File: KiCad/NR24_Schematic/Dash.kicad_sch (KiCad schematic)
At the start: 11 parts, among them J9 AEM Dash, SW2 Shifter Switch, SW5 Key Switch, SW6 12V E-stop

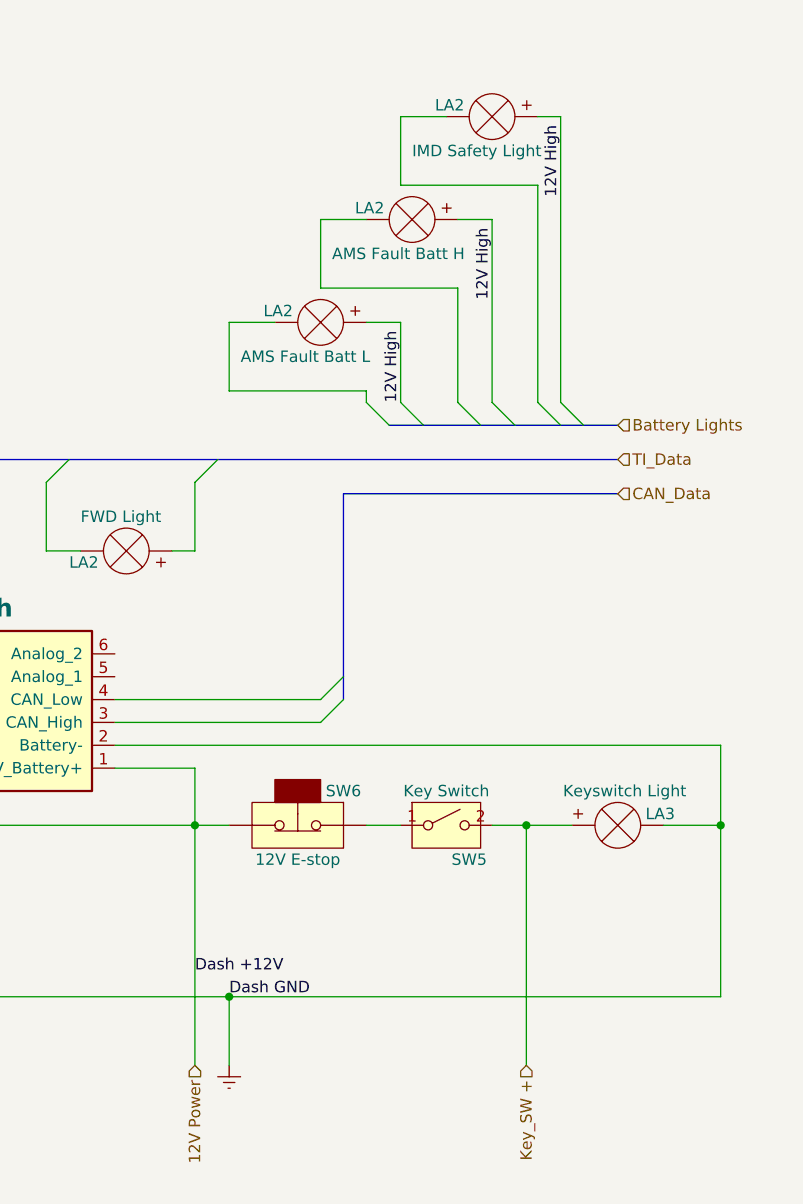
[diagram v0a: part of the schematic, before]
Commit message: added accumulator info
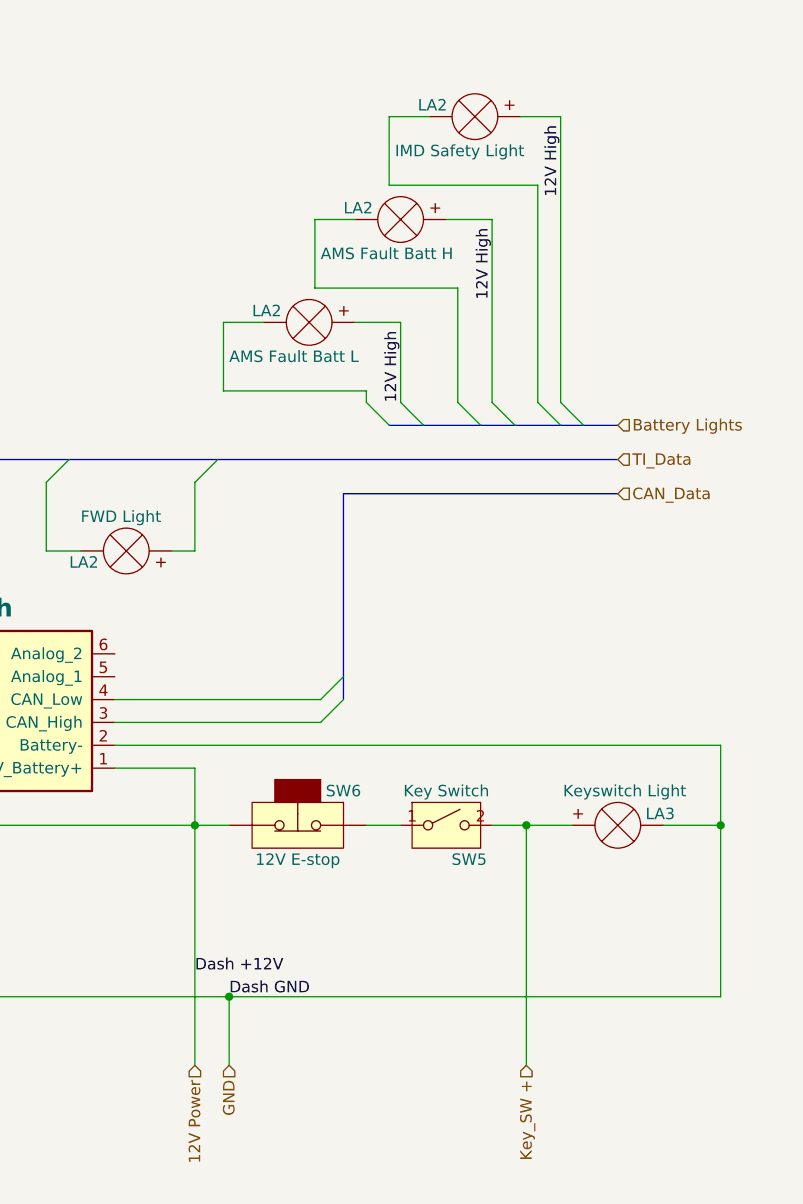
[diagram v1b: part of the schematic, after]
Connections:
- net Earth renamed GND
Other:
- moved on the sheet: LA2
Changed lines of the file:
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@@
     (stroke (width 0) (type default))
   )
-  (wire (pts (xy 187.96 46.99) (xy 187.96 54.61))
+  (wire (pts (xy 187.325 46.99) (xy 187.325 54.61))
     (stroke (width 0) (type default))
   )
@@
     (stroke (width 0) (type default))
   )
-  (wire (pts (xy 217.17 35.56) (xy 213.36 35.56))
+  (wire (pts (xy 217.17 35.56) (xy 212.09 35.56))
     (stroke (width 0) (type default))
   )
@@
     (stroke (width 0) (type default))
   )
-  (wire (pts (xy 187.96 54.61) (xy 203.2 54.61))
-    (stroke (width 0) (type default))
-  )
-  (wire (pts (xy 193.04 46.99) (xy 187.96 46.99))
+  (wire (pts (xy 187.325 54.61) (xy 203.2 54.61))
+    (stroke (width 0) (type default))
+  )
+  (wire (pts (xy 191.77 46.99) (xy 187.325 46.99))
     (stroke (width 0) (type default))
   )
@@
     (stroke (width 0) (type default))
   )
-  (wire (pts (xy 198.12 43.18) (xy 213.36 43.18))
+  (wire (pts (xy 197.485 43.18) (xy 213.36 43.18))
     (stroke (width 0) (type default))
   )
@@
     (stroke (width 0) (type default))
   )
-  (wire (pts (xy 207.01 24.13) (xy 207.01 31.75))
+  (wire (pts (xy 205.74 24.13) (xy 205.74 31.75))
     (stroke (width 0) (type default))
   )
@@
     (stroke (width 0) (type default))
   )
-  (wire (pts (xy 198.12 35.56) (xy 198.12 43.18))
-    (stroke (width 0) (type default))
-  )
-  (wire (pts (xy 222.25 24.13) (xy 224.79 24.13))
+  (wire (pts (xy 197.485 35.56) (xy 197.485 43.18))
+    (stroke (width 0) (type default))
+  )
+  (wire (pts (xy 220.345 24.13) (xy 224.79 24.13))
     (stroke (width 0) (type default))
   )
@@
     (stroke (width 0) (type default))
   )
-  (wire (pts (xy 207.01 46.99) (xy 203.2 46.99))
+  (wire (pts (xy 207.01 46.99) (xy 201.93 46.99))
     (stroke (width 0) (type default))
   )
@@
     (stroke (width 0) (type default))
   )
-  (wire (pts (xy 212.09 24.13) (xy 207.01 24.13))
-    (stroke (width 0) (type default))
-  )
-  (wire (pts (xy 207.01 31.75) (xy 222.25 31.75))
+  (wire (pts (xy 210.185 24.13) (xy 205.74 24.13))
+    (stroke (width 0) (type default))
+  )
+  (wire (pts (xy 205.74 31.75) (xy 222.25 31.75))
     (stroke (width 0) (type default))
   )
@@
     (stroke (width 0) (type default))
   )
-  (wire (pts (xy 203.2 35.56) (xy 198.12 35.56))
+  (wire (pts (xy 201.93 35.56) (xy 197.485 35.56))
     (stroke (width 0) (type default))
   )
@@
     (effects (font (size 1.27 1.27)) (justify right))
   )
+  (hierarchical_label "GND" (shape input) (at 187.96 129.54 270) (fields_autoplaced)
+    (effects (font (size 1.27 1.27)) (justify right))
+  )
   (hierarchical_label "CAN_Data" (shape input) (at 231.14 66.04 0) (fields_autoplaced)
     (effects (font (size 1.27 1.27)) (justify left))
@@
     (pin "2")
     (instances
-      (project "Car_TractiveSystem_v2"
+      (project "Car_TractiveSystem_MAIN"
         (path "/588b5c14-1813-4e1d-9dbe-940839ecebe3"
           (reference "LA3") (unit 1)
@@
     (pin "2")
     (instances
-      (project "Car_TractiveSystem_v2"
+      (project "Car_TractiveSystem_MAIN"
         (path "/588b5c14-1813-4e1d-9dbe-940839ecebe3"
           (reference "SW5") (unit 1)
@@
     (pin "2")
     (instances
-      (project "Car_TractiveSystem_v2"
+      (project "Car_TractiveSystem_MAIN"
         (path "/588b5c14-1813-4e1d-9dbe-940839ecebe3"
           (reference "LA2") (unit 1)
@@
     )
   )
-  (symbol (lib_name "Lamp_2") (lib_id "Device:Lamp") (at 187.96 48.26 0) (mirror y) (unit 1)
-    (in_bom yes) (on_board yes) (dnp no)
-    (property "Reference" "LA2" (at 191.77 45.72 0)
-      (effects (font (size 1.27 1.27)) (justify right))
-    )
-    (property "Value" "AMS Fault Batt L" (at 189.23 50.8 0)
-      (effects (font (size 1.27 1.27)) (justify right))
-    )
-    (property "Footprint" "" (at 195.58 46.99 0)
-      (effects (font (size 1.27 1.27)) hide)
-    )
-    (property "Datasheet" "~" (at 195.58 46.99 0)
-      (effects (font (size 1.27 1.27)) hide)
-    )
-    (pin "1")
-    (pin "2")
-    (instances
-      (project "Car_TractiveSystem_v2"
+  (symbol (lib_name "Lamp_2") (lib_id "Device:Lamp") (at 186.69 48.26 0) (mirror y) (unit 1)
+    (in_bom yes) (on_board yes) (dnp no)
+    (property "Reference" "LA2" (at 190.5 45.72 0)
+      (effects (font (size 1.27 1.27)) (justify right))
+    )
+    (property "Value" "AMS Fault Batt L" (at 187.96 50.8 0)
+      (effects (font (size 1.27 1.27)) (justify right))
+    )
+    (property "Footprint" "" (at 194.31 46.99 0)
+      (effects (font (size 1.27 1.27)) hide)
+    )
+    (property "Datasheet" "~" (at 194.31 46.99 0)
+      (effects (font (size 1.27 1.27)) hide)
+    )
+    (pin "1")
+    (pin "2")
+    (instances
+      (project "Car_TractiveSystem_MAIN"
         (path "/588b5c14-1813-4e1d-9dbe-940839ecebe3"
           (reference "LA2") (unit 1)
@@
     (pin "8")
     (instances
-      (project "Car_TractiveSystem_v2"
+      (project "Car_TractiveSystem_MAIN"
         (path "/588b5c14-1813-4e1d-9dbe-940839ecebe3"
           (reference "SW2") (unit 1)
@@
     (pin "2")
     (instances
-      (project "Car_TractiveSystem_v2"
+      (project "Car_TractiveSystem_MAIN"
         (path "/588b5c14-1813-4e1d-9dbe-940839ecebe3"
           (reference "LA5") (unit 1)
@@
     (pin "2")
     (instances
-      (project "Car_TractiveSystem_v2"
+      (project "Car_TractiveSystem_MAIN"
         (path "/588b5c14-1813-4e1d-9dbe-940839ecebe3"
           (reference "LA1") (unit 1)
@@
     (pin "2")
     (instances
-      (project "Car_TractiveSystem_v2"
+      (project "Car_TractiveSystem_MAIN"
         (path "/588b5c14-1813-4e1d-9dbe-940839ecebe3"
           (reference "SW6") (unit 1)
@@
     )
   )
-  (symbol (lib_id "power:Earth") (at 187.96 129.54 0) (unit 1)
-    (in_bom yes) (on_board yes) (dnp no) (fields_autoplaced)
-    (property "Reference" "#PWR01" (at 187.96 135.89 0)
-      (effects (font (size 1.27 1.27)) hide)
-    )
-    (property "Value" "Earth" (at 187.96 133.35 0)
-      (effects (font (size 1.27 1.27)) hide)
-    )
-    (property "Footprint" "" (at 187.96 129.54 0)
-      (effects (font (size 1.27 1.27)) hide)
-    )
-    (property "Datasheet" "~" (at 187.96 129.54 0)
-      (effects (font (size 1.27 1.27)) hide)
-    )
-    (pin "1")
-    (instances
-      (project "Car_TractiveSystem_v2"
-        (path "/588b5c14-1813-4e1d-9dbe-940839ecebe3"
-          (reference "#PWR01") (unit 1)
-        )
-        (path "/588b5c14-1813-4e1d-9dbe-940839ecebe3/62b4fa84-4530-4bff-bc03-eb6ea850cb52"
-          (reference "#PWR05") (unit 1)
-        )
-      )
-    )
-  )
-  (symbol (lib_name "Lamp_2") (lib_id "Device:Lamp") (at 207.01 25.4 0) (mirror y) (unit 1)
-    (in_bom yes) (on_board yes) (dnp no)
-    (property "Reference" "LA2" (at 210.82 22.86 0)
-      (effects (font (size 1.27 1.27)) (justify right))
-    )
-    (property "Value" "IMD Safety Light" (at 208.28 27.94 0)
-      (effects (font (size 1.27 1.27)) (justify right))
-    )
-    (property "Footprint" "" (at 214.63 24.13 0)
-      (effects (font (size 1.27 1.27)) hide)
-    )
-    (property "Datasheet" "~" (at 214.63 24.13 0)
-      (effects (font (size 1.27 1.27)) hide)
-    )
-    (pin "1")
-    (pin "2")
-    (instances
-      (project "Car_TractiveSystem_v2"
+  (symbol (lib_name "Lamp_2") (lib_id "Device:Lamp") (at 205.105 25.4 0) (mirror y) (unit 1)
+    (in_bom yes) (on_board yes) (dnp no)
+    (property "Reference" "LA2" (at 208.915 22.86 0)
+      (effects (font (size 1.27 1.27)) (justify right))
+    )
+    (property "Value" "IMD Safety Light" (at 206.375 27.94 0)
+      (effects (font (size 1.27 1.27)) (justify right))
+    )
+    (property "Footprint" "" (at 212.725 24.13 0)
+      (effects (font (size 1.27 1.27)) hide)
+    )
+    (property "Datasheet" "~" (at 212.725 24.13 0)
+      (effects (font (size 1.27 1.27)) hide)
+    )
+    (pin "1")
+    (pin "2")
+    (instances
+      (project "Car_TractiveSystem_MAIN"
         (path "/588b5c14-1813-4e1d-9dbe-940839ecebe3"
           (reference "LA2") (unit 1)
@@
     (pin "9")
     (instances
-      (project "Car_TractiveSystem_v2"
+      (project "Car_TractiveSystem_MAIN"
         (path "/588b5c14-1813-4e1d-9dbe-940839ecebe3/62b4fa84-4530-4bff-bc03-eb6ea850cb52"
           (reference "J9") (unit 1)
@@
     )
   )
-  (symbol (lib_name "Lamp_2") (lib_id "Device:Lamp") (at 198.12 36.83 0) (mirror y) (unit 1)
-    (in_bom yes) (on_board yes) (dnp no)
-    (property "Reference" "LA2" (at 201.93 34.29 0)
-      (effects (font (size 1.27 1.27)) (justify right))
-    )
-    (property "Value" "AMS Fault Batt H" (at 199.39 39.37 0)
-      (effects (font (size 1.27 1.27)) (justify right))
-    )
-    (property "Footprint" "" (at 205.74 35.56 0)
-      (effects (font (size 1.27 1.27)) hide)
-    )
-    (property "Datasheet" "~" (at 205.74 35.56 0)
-      (effects (font (size 1.27 1.27)) hide)
-    )
-    (pin "1")
-    (pin "2")
-    (instances
-      (project "Car_TractiveSystem_v2"
+  (symbol (lib_name "Lamp_2") (lib_id "Device:Lamp") (at 196.85 36.83 0) (mirror y) (unit 1)
+    (in_bom yes) (on_board yes) (dnp no)
+    (property "Reference" "LA2" (at 200.66 34.29 0)
+      (effects (font (size 1.27 1.27)) (justify right))
+    )
+    (property "Value" "AMS Fault Batt H" (at 198.12 39.37 0)
+      (effects (font (size 1.27 1.27)) (justify right))
+    )
+    (property "Footprint" "" (at 204.47 35.56 0)
+      (effects (font (size 1.27 1.27)) hide)
+    )
+    (property "Datasheet" "~" (at 204.47 35.56 0)
+      (effects (font (size 1.27 1.27)) hide)
+    )
+    (pin "1")
+    (pin "2")
+    (instances
+      (project "Car_TractiveSystem_MAIN"
         (path "/588b5c14-1813-4e1d-9dbe-940839ecebe3"
           (reference "LA2") (unit 1)

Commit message: Pre Break Schematic
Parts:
- renumbered J9 to J15
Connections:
- removed net 12V High: LA2.2 (+), LA2.2 (+), LA2.2 (+)
- net Rocker 1: no longer names the net of SW2.1
- net Rocker 2: no longer names the net of SW2.2
- net Rocker 3: no longer names the net of SW2.3
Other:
- note added: "12V High"
- note added: "Dash +12V"
- note added: "Dash Ground"
- note added: "Rocker 1"
- note added: "Rocker 2"
- note added: "Rocker 3"
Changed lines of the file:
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@@
+    (stroke (width 0) (type default))
+  )
+  (wire (pts (xy 184.15 102.87) (xy 184.15 129.54))
     (stroke (width 0) (type default))
   )
@@
     (stroke (width 0) (type default))
   )
-  (wire (pts (xy 184.15 102.87) (xy 184.15 129.54))
-    (stroke (width 0) (type default))
-  )
   (wire (pts (xy 217.17 35.56) (xy 212.09 35.56))
     (stroke (width 0) (type default))
@@
     (stroke (width 0) (type default))
   )
+  (text "Dash +12V" (at 182.245 111.76 0)
+    (effects (font (size 1.27 1.27)) (justify right bottom))
+  )
+  (text "12V High" (at 206.375 57.15 90)
+    (effects (font (size 1.27 1.27)) (justify left bottom))
+  )
+  (text "Rocker 3" (at 130.81 80.645 90)
+    (effects (font (size 1.27 1.27)) (justify left bottom))
+  )
   (text "|\\--/|\n| o_o |\n \\_ ^_/" (at 12.7 27.94 0)
     (effects (font (size 3 3)) (justify left bottom))
   )
+  (text "12V High" (at 216.535 46.355 90)
+    (effects (font (size 1.27 1.27)) (justify left bottom))
+  )
+  (text "Rocker 1" (at 127 74.93 90)
+    (effects (font (size 1.27 1.27)) (justify left bottom))
+  )
+  (text "Dash Ground" (at 194.31 120.65 0)
+    (effects (font (size 1.27 1.27)) (justify left bottom))
+  )
+  (text "Rocker 2" (at 106.68 78.105 90)
+    (effects (font (size 1.27 1.27)) (justify left bottom))
+  )
   (text "DASH" (at 134.62 58.42 0)
     (effects (font (size 4 4) (thickness 0.8) bold) (justify left bottom))
   )
-  (label "Dash +12V" (at 184.15 119.38 0) (fields_autoplaced)
-    (effects (font (size 1.27 1.27)) (justify left bottom))
-  )
-  (label "Rocker 2" (at 107.95 76.2 90) (fields_autoplaced)
-    (effects (font (size 1.27 1.27)) (justify left bottom))
-  )
-  (label "Rocker 3" (at 132.08 80.01 90) (fields_autoplaced)
-    (effects (font (size 1.27 1.27)) (justify left bottom))
-  )
-  (label "12V High" (at 207.01 55.88 90) (fields_autoplaced)
-    (effects (font (size 1.27 1.27)) (justify left bottom))
-  )
-  (label "12V High" (at 224.79 33.02 90) (fields_autoplaced)
-    (effects (font (size 1.27 1.27)) (justify left bottom))
-  )
-  (label "Rocker 1" (at 128.27 76.2 90) (fields_autoplaced)
-    (effects (font (size 1.27 1.27)) (justify left bottom))
-  )
-  (label "Dash GND" (at 187.96 121.92 0) (fields_autoplaced)
-    (effects (font (size 1.27 1.27)) (justify left bottom))
-  )
-  (label "12V High" (at 217.17 44.45 90) (fields_autoplaced)
+  (text "12V High" (at 224.155 34.29 90)
     (effects (font (size 1.27 1.27)) (justify left bottom))
   )
@@
     (pin "2")
     (instances
-      (project "Car_TractiveSystem_MAIN"
+      (project "NR24_Schematic"
         (path "/588b5c14-1813-4e1d-9dbe-940839ecebe3"
           (reference "LA3") (unit 1)
         )
         (path "/588b5c14-1813-4e1d-9dbe-940839ecebe3/62b4fa84-4530-4bff-bc03-eb6ea850cb52"
-          (reference "LA4") (unit 1)
+          (reference "LA9") (unit 1)
         )
       )
@@
     (pin "2")
     (instances
-      (project "Car_TractiveSystem_MAIN"
+      (project "NR24_Schematic"
         (path "/588b5c14-1813-4e1d-9dbe-940839ecebe3"
           (reference "SW5") (unit 1)
         )
         (path "/588b5c14-1813-4e1d-9dbe-940839ecebe3/62b4fa84-4530-4bff-bc03-eb6ea850cb52"
-          (reference "SW5") (unit 1)
+          (reference "SW8") (unit 1)
         )
       )
@@
     (pin "2")
     (instances
-      (project "Car_TractiveSystem_MAIN"
+      (project "NR24_Schematic"
         (path "/588b5c14-1813-4e1d-9dbe-940839ecebe3"
           (reference "LA2") (unit 1)
         )
         (path "/588b5c14-1813-4e1d-9dbe-940839ecebe3/62b4fa84-4530-4bff-bc03-eb6ea850cb52"
+          (reference "LA6") (unit 1)
+        )
+      )
+    )
+  )
+  (symbol (lib_name "Lamp_2") (lib_id "Device:Lamp") (at 186.69 48.26 0) (mirror y) (unit 1)
+    (in_bom yes) (on_board yes) (dnp no)
+    (property "Reference" "LA2" (at 190.5 45.72 0)
+      (effects (font (size 1.27 1.27)) (justify right))
+    )
+    (property "Value" "AMS Fault Batt L" (at 187.96 50.8 0)
+      (effects (font (size 1.27 1.27)) (justify right))
+    )
+    (property "Footprint" "" (at 194.31 46.99 0)
+      (effects (font (size 1.27 1.27)) hide)
+    )
+    (property "Datasheet" "~" (at 194.31 46.99 0)
+      (effects (font (size 1.27 1.27)) hide)
+    )
+    (pin "1")
+    (pin "2")
+    (instances
+      (project "NR24_Schematic"
+        (path "/588b5c14-1813-4e1d-9dbe-940839ecebe3"
           (reference "LA2") (unit 1)
         )
-      )
-    )
-  )
-  (symbol (lib_name "Lamp_2") (lib_id "Device:Lamp") (at 186.69 48.26 0) (mirror y) (unit 1)
-    (in_bom yes) (on_board yes) (dnp no)
-    (property "Reference" "LA2" (at 190.5 45.72 0)
-      (effects (font (size 1.27 1.27)) (justify right))
-    )
-    (property "Value" "AMS Fault Batt L" (at 187.96 50.8 0)
-      (effects (font (size 1.27 1.27)) (justify right))
-    )
-    (property "Footprint" "" (at 194.31 46.99 0)
-      (effects (font (size 1.27 1.27)) hide)
-    )
-    (property "Datasheet" "~" (at 194.31 46.99 0)
-      (effects (font (size 1.27 1.27)) hide)
-    )
-    (pin "1")
-    (pin "2")
-    (instances
-      (project "Car_TractiveSystem_MAIN"
-        (path "/588b5c14-1813-4e1d-9dbe-940839ecebe3"
-          (reference "LA2") (unit 1)
-        )
-        (path "/588b5c14-1813-4e1d-9dbe-940839ecebe3/62b4fa84-4530-4bff-bc03-eb6ea850cb52"
-          (reference "LA9") (unit 1)
+        (path "/588b5c14-1813-4e1d-9dbe-940839ecebe3/62b4fa84-4530-4bff-bc03-eb6ea850cb52"
+          (reference "LA5") (unit 1)
         )
       )
@@
     (pin "8")
     (instances
-      (project "Car_TractiveSystem_MAIN"
+      (project "NR24_Schematic"
         (path "/588b5c14-1813-4e1d-9dbe-940839ecebe3"
           (reference "SW2") (unit 1)
         )
         (path "/588b5c14-1813-4e1d-9dbe-940839ecebe3/62b4fa84-4530-4bff-bc03-eb6ea850cb52"
-          (reference "SW2") (unit 1)
+          (reference "SW6") (unit 1)
         )
       )
@@
     (pin "2")
     (instances
-      (project "Car_TractiveSystem_MAIN"
+      (project "NR24_Schematic"
         (path "/588b5c14-1813-4e1d-9dbe-940839ecebe3"
           (reference "LA5") (unit 1)
         )
         (path "/588b5c14-1813-4e1d-9dbe-940839ecebe3/62b4fa84-4530-4bff-bc03-eb6ea850cb52"
-          (reference "LA3") (unit 1)
+          (reference "LA8") (unit 1)
         )
       )
@@
     (pin "2")
     (instances
-      (project "Car_TractiveSystem_MAIN"
+      (project "NR24_Schematic"
         (path "/588b5c14-1813-4e1d-9dbe-940839ecebe3"
           (reference "LA1") (unit 1)
         )
         (path "/588b5c14-1813-4e1d-9dbe-940839ecebe3/62b4fa84-4530-4bff-bc03-eb6ea850cb52"
-          (reference "LA1") (unit 1)
+          (reference "LA7") (unit 1)
         )
       )
@@
     (pin "2")
     (instances
-      (project "Car_TractiveSystem_MAIN"
+      (project "NR24_Schematic"
         (path "/588b5c14-1813-4e1d-9dbe-940839ecebe3"
           (reference "SW6") (unit 1)
         )
         (path "/588b5c14-1813-4e1d-9dbe-940839ecebe3/62b4fa84-4530-4bff-bc03-eb6ea850cb52"
-          (reference "SW6") (unit 1)
+          (reference "SW7") (unit 1)
         )
       )
@@
     (pin "2")
     (instances
-      (project "Car_TractiveSystem_MAIN"
+      (project "NR24_Schematic"
         (path "/588b5c14-1813-4e1d-9dbe-940839ecebe3"
           (reference "LA2") (unit 1)
         )
         (path "/588b5c14-1813-4e1d-9dbe-940839ecebe3/62b4fa84-4530-4bff-bc03-eb6ea850cb52"
-          (reference "LA7") (unit 1)
+          (reference "LA3") (unit 1)
         )
       )
@@
   (symbol (lib_id "NR24_Car:AVR-TPI-6") (at 156.21 90.17 0) (mirror x) (unit 1)
     (in_bom yes) (on_board yes) (dnp no)
-    (property "Reference" "J9" (at 156.845 104.14 0)
+    (property "Reference" "J15" (at 156.845 104.14 0)
       (effects (font (size 1.27 1.27)) hide)
     )
@@
     (pin "9")
     (instances
-      (project "Car_TractiveSystem_MAIN"
-        (path "/588b5c14-1813-4e1d-9dbe-940839ecebe3/62b4fa84-4530-4bff-bc03-eb6ea850cb52"
-          (reference "J9") (unit 1)
+      (project "NR24_Schematic"
+        (path "/588b5c14-1813-4e1d-9dbe-940839ecebe3/62b4fa84-4530-4bff-bc03-eb6ea850cb52"
+          (reference "J15") (unit 1)
         )
       )
@@
     (pin "2")
     (instances
-      (project "Car_TractiveSystem_MAIN"
+      (project "NR24_Schematic"
         (path "/588b5c14-1813-4e1d-9dbe-940839ecebe3"
           (reference "LA2") (unit 1)
         )
         (path "/588b5c14-1813-4e1d-9dbe-940839ecebe3/62b4fa84-4530-4bff-bc03-eb6ea850cb52"
-          (reference "LA8") (unit 1)
-        )
-      )
+          (reference "LA4") (unit 1)
+        )
+      )
